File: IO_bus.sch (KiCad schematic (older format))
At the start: 3 parts, among them P10 CONN_01X08, P9 CONN_01X14

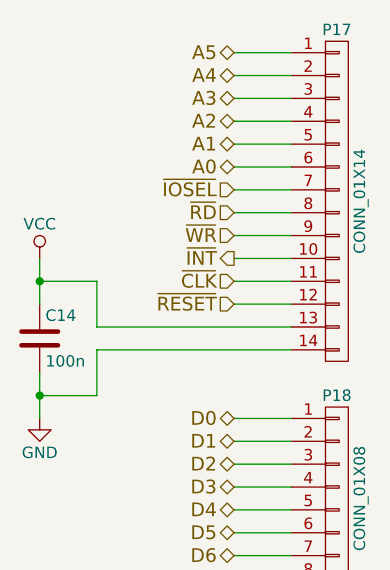
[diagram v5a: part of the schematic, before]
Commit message: Updated LEDs, added power supply options, added mounting holes in schematic.
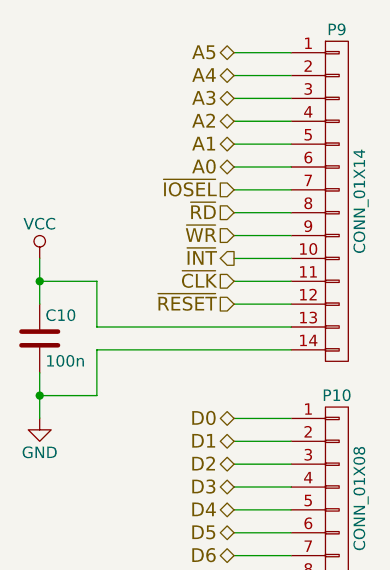
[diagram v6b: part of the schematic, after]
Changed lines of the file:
@@
 LIBS:microchip_pic18mcu
 LIBS:6850
+LIBS:nrc2016
 LIBS:z80-cache
 EELAYER 25 0
@@
 $Descr A4 11693 8268
 encoding utf-8
-Sheet 8 16
+Sheet 4 16
 Title ""
 Date ""
@@
 AR Path="/578460AE/57973E0B/57809978" Ref="P22"  Part="1"
 AR Path="/578460AE/57974892/57809978" Ref="P24"  Part="1"
-F 0 "P18" H 3700 4400 50  0000 C CNN
+F 0 "P10" H 3700 4400 50  0000 C CNN
 F 1 "CONN_01X08" V 3800 3950 50  0000 C CNN
 F 2 "Pin_Headers:Pin_Header_Straight_1x08" H 3700 3950 50  0001 C CNN
@@
 AR Path="/578460AE/57973E0B/5783B273" Ref="#PWR042"  Part="1"
 AR Path="/578460AE/57974892/5783B273" Ref="#PWR044"  Part="1"
-F 0 "#PWR044" H 2400 2750 50  0001 C CNN
+F 0 "#PWR030" H 2400 2750 50  0001 C CNN
 F 1 "VCC" H 2400 3050 50  0000 C CNN
 F 2 "" H 2400 2900 50  0000 C CNN
@@
 AR Path="/578460AE/57973E0B/5783B28B" Ref="#PWR043"  Part="1"
 AR Path="/578460AE/57974892/5783B28B" Ref="#PWR045"  Part="1"
-F 0 "#PWR045" H 2400 3350 50  0001 C CNN
+F 0 "#PWR031" H 2400 3350 50  0001 C CNN
 F 1 "GND" H 2400 3450 50  0000 C CNN
 F 2 "" H 2400 3600 50  0000 C CNN
@@
 AR Path="/578460AE/57973E0B/5783B2B3" Ref="C16"  Part="1"
 AR Path="/578460AE/57974892/5783B2B3" Ref="C17"  Part="1"
-F 0 "C14" H 2425 3350 50  0000 L CNN
+F 0 "C10" H 2425 3350 50  0000 L CNN
 F 1 "100n" H 2425 3150 50  0000 L CNN
 F 2 "Capacitors_SMD:C_0805_HandSoldering" H 2438 3100 50  0001 C CNN
@@
 AR Path="/578460AE/57973E0B/5796F695" Ref="P21"  Part="1"
 AR Path="/578460AE/57974892/5796F695" Ref="P23"  Part="1"
-F 0 "P17" H 3700 3400 50  0000 C CNN
+F 0 "P9" H 3700 3400 50  0000 C CNN
 F 1 "CONN_01X14" V 3800 2650 50  0000 C CNN
 F 2 "Socket_Strips:Socket_Strip_Straight_1x14" H 3700 2650 50  0001 C CNN

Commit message: Update PCB, better layout. Got Addr bus back in order
Think having both USB and DC input would be useful. Switchmode a plus
then plugpack/battery etc voltage doesn't matter. Plus I have a bag full
of those parts too!

I've refdes'd the linear reg just to deal with the net. Will remove if
we both are happy with switcher. Linear cheaper to kit out I guess.

Was trying to find a better way to combine USB and DC power rails than
just schottky diodes. If you have any ideas.

Going to have a big area under the IO ports, might be worth adding a USB
to serial, or sacrifice a IO port for some blinky LEDs and buttons?
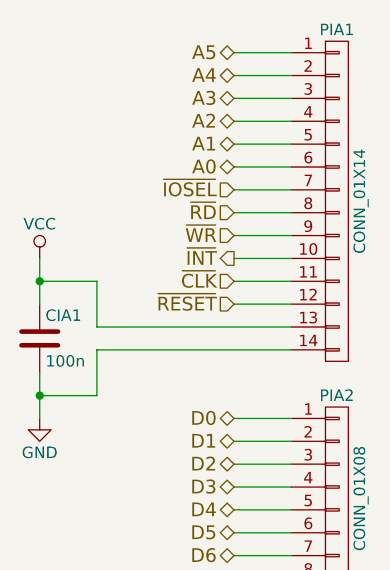
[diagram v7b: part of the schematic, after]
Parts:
- PIA2: renamed from P10; footprint Pin_Headers:Pin_Header_Straight_1x08 -> Socket_Strips:Socket_Strip_Straight_1x08
- renumbered C10 to CIA1, P9 to PIA1
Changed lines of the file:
@@
 	2650 3300 3500 3300
 $Comp
-L CONN_01X08 P10
+L CONN_01X08 PIA2
 U 1 1 57809978
 P 3700 3950
-AR Path="/578460AE/578087DE/57809978" Ref="P10"  Part="1"
-AR Path="/578460AE/57822535/57809978" Ref="P12"  Part="1"
-AR Path="/578460AE/57824229/57809978" Ref="P14"  Part="1"
-AR Path="/578460AE/57824279/57809978" Ref="P16"  Part="1"
-AR Path="/578460AE/578298A9/57809978" Ref="P18"  Part="1"
-AR Path="/578460AE/578298F9/57809978" Ref="P20"  Part="1"
-AR Path="/578460AE/57830D91/57809978" Ref="P22"  Part="1"
-AR Path="/578460AE/57831F66/57809978" Ref="P24"  Part="1"
-AR Path="/578460AE/57951EDB/57809978" Ref="P12"  Part="1"
-AR Path="/578460AE/57952CC1/57809978" Ref="P14"  Part="1"
-AR Path="/578460AE/579537DA/57809978" Ref="P16"  Part="1"
-AR Path="/578460AE/579543C3/57809978" Ref="P18"  Part="1"
-AR Path="/578460AE/57954FF1/57809978" Ref="P20"  Part="1"
-AR Path="/578460AE/57955FE5/57809978" Ref="P22"  Part="1"
-AR Path="/578460AE/57956D49/57809978" Ref="P24"  Part="1"
-AR Path="/578460AE/57970A38/57809978" Ref="P12"  Part="1"
-AR Path="/578460AE/57971583/57809978" Ref="P14"  Part="1"
-AR Path="/578460AE/579727D6/57809978" Ref="P16"  Part="1"
-AR Path="/578460AE/57972DE9/57809978" Ref="P18"  Part="1"
-AR Path="/578460AE/579734B0/57809978" Ref="P20"  Part="1"
-AR Path="/578460AE/57973E0B/57809978" Ref="P22"  Part="1"
-AR Path="/578460AE/57974892/57809978" Ref="P24"  Part="1"
-F 0 "P10" H 3700 4400 50  0000 C CNN
+AR Path="/578460AE/578087DE/57809978" Ref="PIA2"  Part="1"
+AR Path="/578460AE/57970A38/57809978" Ref="PIG2"  Part="1"
+AR Path="/578460AE/57971583/57809978" Ref="PIH2"  Part="1"
+AR Path="/578460AE/579727D6/57809978" Ref="PIB2"  Part="1"
+AR Path="/578460AE/57972DE9/57809978" Ref="PIC2"  Part="1"
+AR Path="/578460AE/579734B0/57809978" Ref="PID2"  Part="1"
+AR Path="/578460AE/57973E0B/57809978" Ref="PIE2"  Part="1"
+AR Path="/578460AE/57974892/57809978" Ref="PIF2"  Part="1"
+F 0 "PIA2" H 3700 4400 50  0000 C CNN
 F 1 "CONN_01X08" V 3800 3950 50  0000 C CNN
-F 2 "Pin_Headers:Pin_Header_Straight_1x08" H 3700 3950 50  0001 C CNN
+F 2 "Socket_Strips:Socket_Strip_Straight_1x08" H 3700 3950 50  0001 C CNN
 F 3 "" H 3700 3950 50  0000 C CNN
 	1    3700 3950
@@
 	2400 3400 2400 3600
 $Comp
-L VCC #PWR030
+L VCC #PWR041
 U 1 1 5783B273
 P 2400 2900
-AR Path="/578460AE/578087DE/5783B273" Ref="#PWR030"  Part="1"
-AR Path="/578460AE/57822535/5783B273" Ref="#PWR029"  Part="1"
-AR Path="/578460AE/57824229/5783B273" Ref="#PWR031"  Part="1"
-AR Path="/578460AE/57824279/5783B273" Ref="#PWR033"  Part="1"
-AR Path="/578460AE/578298A9/5783B273" Ref="#PWR035"  Part="1"
-AR Path="/578460AE/578298F9/5783B273" Ref="#PWR037"  Part="1"
-AR Path="/578460AE/57830D91/5783B273" Ref="#PWR039"  Part="1"
-AR Path="/578460AE/57831F66/5783B273" Ref="#PWR041"  Part="1"
-AR Path="/578460AE/57951EDB/5783B273" Ref="#PWR28"  Part="1"
-AR Path="/578460AE/57952CC1/5783B273" Ref="#PWR30"  Part="1"
-AR Path="/578460AE/579537DA/5783B273" Ref="#PWR32"  Part="1"
-AR Path="/578460AE/579543C3/5783B273" Ref="#PWR34"  Part="1"
-AR Path="/578460AE/57954FF1/5783B273" Ref="#PWR36"  Part="1"
-AR Path="/578460AE/57955FE5/5783B273" Ref="#PWR38"  Part="1"
-AR Path="/578460AE/57956D49/5783B273" Ref="#PWR40"  Part="1"
-AR Path="/578460AE/57970A38/5783B273" Ref="#PWR032"  Part="1"
-AR Path="/578460AE/57971583/5783B273" Ref="#PWR034"  Part="1"
-AR Path="/578460AE/579727D6/5783B273" Ref="#PWR036"  Part="1"
-AR Path="/578460AE/57972DE9/5783B273" Ref="#PWR038"  Part="1"
-AR Path="/578460AE/579734B0/5783B273" Ref="#PWR040"  Part="1"
-AR Path="/578460AE/57973E0B/5783B273" Ref="#PWR042"  Part="1"
-AR Path="/578460AE/57974892/5783B273" Ref="#PWR044"  Part="1"
-F 0 "#PWR030" H 2400 2750 50  0001 C CNN
+AR Path="/578460AE/578087DE/5783B273" Ref="#PWR041"  Part="1"
+AR Path="/578460AE/57970A38/5783B273" Ref="#PWR043"  Part="1"
+AR Path="/578460AE/57971583/5783B273" Ref="#PWR045"  Part="1"
+AR Path="/578460AE/579727D6/5783B273" Ref="#PWR047"  Part="1"
+AR Path="/578460AE/57972DE9/5783B273" Ref="#PWR049"  Part="1"
+AR Path="/578460AE/579734B0/5783B273" Ref="#PWR051"  Part="1"
+AR Path="/578460AE/57973E0B/5783B273" Ref="#PWR053"  Part="1"
+AR Path="/578460AE/57974892/5783B273" Ref="#PWR055"  Part="1"
+F 0 "#PWR055" H 2400 2750 50  0001 C CNN
 F 1 "VCC" H 2400 3050 50  0000 C CNN
 F 2 "" H 2400 2900 50  0000 C CNN
@@
 $EndComp
 $Comp
-L GND #PWR031
+L GND #PWR042
 U 1 1 5783B28B
 P 2400 3600
-AR Path="/578460AE/578087DE/5783B28B" Ref="#PWR031"  Part="1"
-AR Path="/578460AE/57822535/5783B28B" Ref="#PWR030"  Part="1"
-AR Path="/578460AE/57824229/5783B28B" Ref="#PWR032"  Part="1"
-AR Path="/578460AE/57824279/5783B28B" Ref="#PWR034"  Part="1"
-AR Path="/578460AE/578298A9/5783B28B" Ref="#PWR036"  Part="1"
-AR Path="/578460AE/578298F9/5783B28B" Ref="#PWR038"  Part="1"
-AR Path="/578460AE/57830D91/5783B28B" Ref="#PWR040"  Part="1"
-AR Path="/578460AE/57831F66/5783B28B" Ref="#PWR042"  Part="1"
-AR Path="/578460AE/57951EDB/5783B28B" Ref="#PWR29"  Part="1"
-AR Path="/578460AE/57952CC1/5783B28B" Ref="#PWR31"  Part="1"
-AR Path="/578460AE/579537DA/5783B28B" Ref="#PWR33"  Part="1"
-AR Path="/578460AE/579543C3/5783B28B" Ref="#PWR35"  Part="1"
-AR Path="/578460AE/57954FF1/5783B28B" Ref="#PWR37"  Part="1"
-AR Path="/578460AE/57955FE5/5783B28B" Ref="#PWR39"  Part="1"
-AR Path="/578460AE/57956D49/5783B28B" Ref="#PWR41"  Part="1"
-AR Path="/578460AE/57970A38/5783B28B" Ref="#PWR033"  Part="1"
-AR Path="/578460AE/57971583/5783B28B" Ref="#PWR035"  Part="1"
-AR Path="/578460AE/579727D6/5783B28B" Ref="#PWR037"  Part="1"
-AR Path="/578460AE/57972DE9/5783B28B" Ref="#PWR039"  Part="1"
-AR Path="/578460AE/579734B0/5783B28B" Ref="#PWR041"  Part="1"
-AR Path="/578460AE/57973E0B/5783B28B" Ref="#PWR043"  Part="1"
-AR Path="/578460AE/57974892/5783B28B" Ref="#PWR045"  Part="1"
-F 0 "#PWR031" H 2400 3350 50  0001 C CNN
+AR Path="/578460AE/578087DE/5783B28B" Ref="#PWR042"  Part="1"
+AR Path="/578460AE/57970A38/5783B28B" Ref="#PWR044"  Part="1"
+AR Path="/578460AE/57971583/5783B28B" Ref="#PWR046"  Part="1"
+AR Path="/578460AE/579727D6/5783B28B" Ref="#PWR048"  Part="1"
+AR Path="/578460AE/57972DE9/5783B28B" Ref="#PWR050"  Part="1"
+AR Path="/578460AE/579734B0/5783B28B" Ref="#PWR052"  Part="1"
+AR Path="/578460AE/57973E0B/5783B28B" Ref="#PWR054"  Part="1"
+AR Path="/578460AE/57974892/5783B28B" Ref="#PWR056"  Part="1"
+F 0 "#PWR056" H 2400 3350 50  0001 C CNN
 F 1 "GND" H 2400 3450 50  0000 C CNN
 F 2 "" H 2400 3600 50  0000 C CNN
@@
 $EndComp
 $Comp
-L C C10
+L C CIA1
 U 1 1 5783B2B3
 P 2400 3250
-AR Path="/578460AE/578087DE/5783B2B3" Ref="C10"  Part="1"
-AR Path="/578460AE/57822535/5783B2B3" Ref="C11"  Part="1"
-AR Path="/578460AE/57824229/5783B2B3" Ref="C12"  Part="1"
-AR Path="/578460AE/57824279/5783B2B3" Ref="C13"  Part="1"
-AR Path="/578460AE/578298A9/5783B2B3" Ref="C14"  Part="1"
-AR Path="/578460AE/578298F9/5783B2B3" Ref="C15"  Part="1"
-AR Path="/578460AE/57830D91/5783B2B3" Ref="C16"  Part="1"
-AR Path="/578460AE/57831F66/5783B2B3" Ref="C17"  Part="1"
-AR Path="/578460AE/57951EDB/5783B2B3" Ref="C10"  Part="1"
-AR Path="/578460AE/57952CC1/5783B2B3" Ref="C10"  Part="1"
-AR Path="/578460AE/579537DA/5783B2B3" Ref="C10"  Part="1"
-AR Path="/578460AE/579543C3/5783B2B3" Ref="C10"  Part="1"
-AR Path="/578460AE/57954FF1/5783B2B3" Ref="C10"  Part="1"
-AR Path="/578460AE/57955FE5/5783B2B3" Ref="C10"  Part="1"
-AR Path="/578460AE/57956D49/5783B2B3" Ref="C10"  Part="1"
-AR Path="/578460AE/57970A38/5783B2B3" Ref="C11"  Part="1"
-AR Path="/578460AE/57971583/5783B2B3" Ref="C12"  Part="1"
-AR Path="/578460AE/579727D6/5783B2B3" Ref="C13"  Part="1"
-AR Path="/578460AE/57972DE9/5783B2B3" Ref="C14"  Part="1"
-AR Path="/578460AE/579734B0/5783B2B3" Ref="C15"  Part="1"
-AR Path="/578460AE/57973E0B/5783B2B3" Ref="C16"  Part="1"
-AR Path="/578460AE/57974892/5783B2B3" Ref="C17"  Part="1"
-F 0 "C10" H 2425 3350 50  0000 L CNN
+AR Path="/578460AE/578087DE/5783B2B3" Ref="CIA1"  Part="1"
+AR Path="/578460AE/57970A38/5783B2B3" Ref="CIG1"  Part="1"
+AR Path="/578460AE/57971583/5783B2B3" Ref="CIH1"  Part="1"
+AR Path="/578460AE/579727D6/5783B2B3" Ref="CIB1"  Part="1"
+AR Path="/578460AE/57972DE9/5783B2B3" Ref="CIC1"  Part="1"
+AR Path="/578460AE/579734B0/5783B2B3" Ref="CID1"  Part="1"
+AR Path="/578460AE/57973E0B/5783B2B3" Ref="CIE1"  Part="1"
+AR Path="/578460AE/57974892/5783B2B3" Ref="CIF1"  Part="1"
+F 0 "CIA1" H 2425 3350 50  0000 L CNN
 F 1 "100n" H 2425 3150 50  0000 L CNN
 F 2 "Capacitors_SMD:C_0805_HandSoldering" H 2438 3100 50  0001 C CNN
@@
 Connection ~ 2400 3500
 $Comp
-L CONN_01X14 P9
+L CONN_01X14 PIA1
 U 1 1 5796F695
 P 3700 2650
-AR Path="/578460AE/578087DE/5796F695" Ref="P9"  Part="1"
-AR Path="/578460AE/57970A38/5796F695" Ref="P11"  Part="1"
-AR Path="/578460AE/57971583/5796F695" Ref="P13"  Part="1"
-AR Path="/578460AE/579727D6/5796F695" Ref="P15"  Part="1"
-AR Path="/578460AE/57972DE9/5796F695" Ref="P17"  Part="1"
-AR Path="/578460AE/579734B0/5796F695" Ref="P19"  Part="1"
-AR Path="/578460AE/57973E0B/5796F695" Ref="P21"  Part="1"
-AR Path="/578460AE/57974892/5796F695" Ref="P23"  Part="1"
-F 0 "P9" H 3700 3400 50  0000 C CNN
+AR Path="/578460AE/578087DE/5796F695" Ref="PIA1"  Part="1"
+AR Path="/578460AE/57970A38/5796F695" Ref="PIG1"  Part="1"
+AR Path="/578460AE/57971583/5796F695" Ref="PIH1"  Part="1"
+AR Path="/578460AE/579727D6/5796F695" Ref="PIB1"  Part="1"
+AR Path="/578460AE/57972DE9/5796F695" Ref="PIC1"  Part="1"
+AR Path="/578460AE/579734B0/5796F695" Ref="PID1"  Part="1"
+AR Path="/578460AE/57973E0B/5796F695" Ref="PIE1"  Part="1"
+AR Path="/578460AE/57974892/5796F695" Ref="PIF1"  Part="1"
+F 0 "PIA1" H 3700 3400 50  0000 C CNN
 F 1 "CONN_01X14" V 3800 2650 50  0000 C CNN
 F 2 "Socket_Strips:Socket_Strip_Straight_1x14" H 3700 2650 50  0001 C CNN

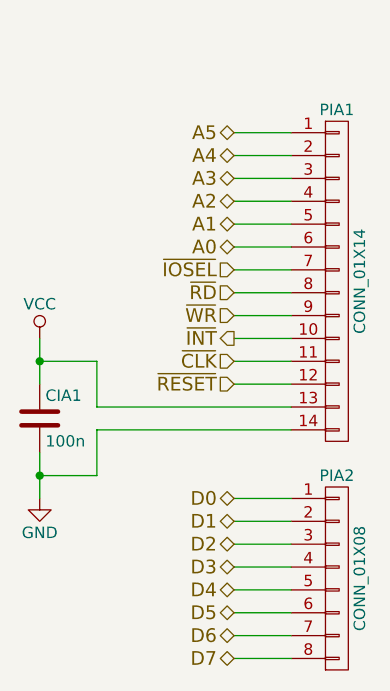
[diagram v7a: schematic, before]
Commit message: PCB layout complete, passes DRC, more tuning required
One thing not enough buffers for all address lines (missed A5), so
swapped out the CLK. Not sure if that was a good idea, but didn't want
to add another chip for a single buffer. :(
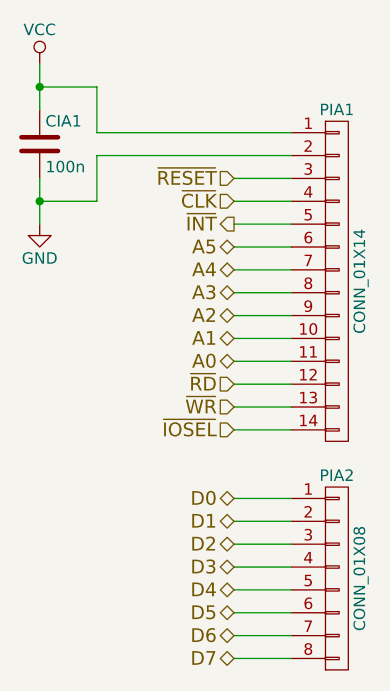
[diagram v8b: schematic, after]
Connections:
- net A0: now also PIA1.11 (P11); no longer PIA1.6 (P6)
- net A1: now also PIA1.10 (P10); no longer PIA1.5 (P5)
- net A2: now also PIA1.9 (P9); no longer PIA1.4 (P4)
- net A3: now also PIA1.8 (P8); no longer PIA1.3 (P3)
- net A4: now also PIA1.7 (P7); no longer PIA1.2 (P2)
- net A5: now also PIA1.6 (P6); no longer PIA1.1 (P1)
- net GND: now also PIA1.2 (P2); no longer PIA1.14 (P14)
- net VCC: now also PIA1.1 (P1); no longer PIA1.13 (P13)
- net ~CLK: now also PIA1.4 (P4); no longer PIA1.11 (P11)
- net ~INT: now also PIA1.5 (P5); no longer PIA1.10 (P10)
- net ~IOSEL: now also PIA1.14 (P14); no longer PIA1.7 (P7)
- net ~RD: now also PIA1.12 (P12); no longer PIA1.8 (P8)
- net ~RESET: now also PIA1.3 (P3); no longer PIA1.12 (P12)
- net ~WR: now also PIA1.13 (P13); no longer PIA1.9 (P9)
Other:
- moved on the sheet: CIA1
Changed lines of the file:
@@
 Comment4 ""
 $EndDescr
+Text HLabel 3250 3000 0    60   3State ~ 0
+A0
+Text HLabel 3250 2900 0    60   3State ~ 0
+A1
+Text HLabel 3250 2800 0    60   3State ~ 0
+A2
+Text HLabel 3250 2700 0    60   3State ~ 0
+A3
+Text HLabel 3250 2600 0    60   3State ~ 0
+A4
 Text HLabel 3250 2500 0    60   3State ~ 0
-A0
-Text HLabel 3250 2400 0    60   3State ~ 0
-A1
-Text HLabel 3250 2300 0    60   3State ~ 0
-A2
-Text HLabel 3250 2200 0    60   3State ~ 0
-A3
-Text HLabel 3250 2100 0    60   3State ~ 0
-A4
-Text HLabel 3250 2000 0    60   3State ~ 0
 A5
-Text HLabel 3250 2600 0    60   Input ~ 0
+Text HLabel 3250 3300 0    60   Input ~ 0
 ~IOSEL
-Text HLabel 3250 2700 0    60   Input ~ 0
+Text HLabel 3250 3100 0    60   Input ~ 0
 ~RD
-Text HLabel 3250 2800 0    60   Input ~ 0
+Text HLabel 3250 3200 0    60   Input ~ 0
 ~WR
-Text HLabel 3250 3000 0    60   Input ~ 0
+Text HLabel 3250 2300 0    60   Input ~ 0
 ~CLK
-Text HLabel 3250 2900 0    60   Output ~ 0
+Text HLabel 3250 2400 0    60   Output ~ 0
 ~INT
 Text HLabel 3250 4000 0    60   BiDi ~ 0
@@
 D3
 Wire Wire Line
-	3250 2000 3500 2000
-Wire Wire Line
-	3500 2100 3250 2100
-Wire Wire Line
-	3250 2200 3500 2200
-Wire Wire Line
-	3500 2300 3250 2300
-Wire Wire Line
 	3250 2400 3500 2400
 Wire Wire Line
@@
 	3250 2800 3500 2800
 Wire Wire Line
-	3250 2900 3500 2900
+	3500 2900 3250 2900
 Wire Wire Line
 	3250 3000 3500 3000
 Wire Wire Line
-	2650 3300 3500 3300
+	3500 3100 3250 3100
+Wire Wire Line
+	3250 3200 3500 3200
+Wire Wire Line
+	3250 3300 3500 3300
+Wire Wire Line
+	3250 2200 3500 2200
+Wire Wire Line
+	2650 2100 3500 2100
 $Comp
 L CONN_01X08 PIA2
@@
 Wire Wire Line
 	3500 4300 3250 4300
-Text HLabel 3250 3100 0    60   Input ~ 0
+Text HLabel 3250 2200 0    60   Input ~ 0
 ~RESET
 Wire Wire Line
-	3250 3100 3500 3100
+	3250 2300 3500 2300
 Wire Wire Line
-	2400 2900 2400 3100
+	2400 1700 2400 1900
 Wire Wire Line
-	2400 3400 2400 3600
+	2400 2200 2400 2400
 $Comp
-L VCC #PWR041
+L VCC #PWR035
 U 1 1 5783B273
-P 2400 2900
-AR Path="/578460AE/578087DE/5783B273" Ref="#PWR041"  Part="1"
-AR Path="/578460AE/57970A38/5783B273" Ref="#PWR043"  Part="1"
-AR Path="/578460AE/57971583/5783B273" Ref="#PWR045"  Part="1"
-AR Path="/578460AE/579727D6/5783B273" Ref="#PWR047"  Part="1"
-AR Path="/578460AE/57972DE9/5783B273" Ref="#PWR049"  Part="1"
-AR Path="/578460AE/579734B0/5783B273" Ref="#PWR051"  Part="1"
-AR Path="/578460AE/57973E0B/5783B273" Ref="#PWR053"  Part="1"
-AR Path="/578460AE/57974892/5783B273" Ref="#PWR055"  Part="1"
-F 0 "#PWR055" H 2400 2750 50  0001 C CNN
-F 1 "VCC" H 2400 3050 50  0000 C CNN
-F 2 "" H 2400 2900 50  0000 C CNN
-F 3 "" H 2400 2900 50  0000 C CNN
-	1    2400 2900
+P 2400 1700
+AR Path="/578460AE/578087DE/5783B273" Ref="#PWR035"  Part="1"
+AR Path="/578460AE/57970A38/5783B273" Ref="#PWR037"  Part="1"
+AR Path="/578460AE/57971583/5783B273" Ref="#PWR039"  Part="1"
+AR Path="/578460AE/579727D6/5783B273" Ref="#PWR041"  Part="1"
+AR Path="/578460AE/57972DE9/5783B273" Ref="#PWR043"  Part="1"
+AR Path="/578460AE/579734B0/5783B273" Ref="#PWR045"  Part="1"
+AR Path="/578460AE/57973E0B/5783B273" Ref="#PWR047"  Part="1"
+AR Path="/578460AE/57974892/5783B273" Ref="#PWR049"  Part="1"
+F 0 "#PWR035" H 2400 1550 50  0001 C CNN
+F 1 "VCC" H 2400 1850 50  0000 C CNN
+F 2 "" H 2400 1700 50  0000 C CNN
+F 3 "" H 2400 1700 50  0000 C CNN
+	1    2400 1700
 	1    0    0    -1
 $EndComp
 $Comp
-L GND #PWR042
+L GND #PWR036
 U 1 1 5783B28B
-P 2400 3600
-AR Path="/578460AE/578087DE/5783B28B" Ref="#PWR042"  Part="1"
-AR Path="/578460AE/57970A38/5783B28B" Ref="#PWR044"  Part="1"
-AR Path="/578460AE/57971583/5783B28B" Ref="#PWR046"  Part="1"
-AR Path="/578460AE/579727D6/5783B28B" Ref="#PWR048"  Part="1"
-AR Path="/578460AE/57972DE9/5783B28B" Ref="#PWR050"  Part="1"
-AR Path="/578460AE/579734B0/5783B28B" Ref="#PWR052"  Part="1"
-AR Path="/578460AE/57973E0B/5783B28B" Ref="#PWR054"  Part="1"
-AR Path="/578460AE/57974892/5783B28B" Ref="#PWR056"  Part="1"
-F 0 "#PWR056" H 2400 3350 50  0001 C CNN
-F 1 "GND" H 2400 3450 50  0000 C CNN
-F 2 "" H 2400 3600 50  0000 C CNN
-F 3 "" H 2400 3600 50  0000 C CNN
-	1    2400 3600
+P 2400 2400
+AR Path="/578460AE/578087DE/5783B28B" Ref="#PWR036"  Part="1"
+AR Path="/578460AE/57970A38/5783B28B" Ref="#PWR038"  Part="1"
+AR Path="/578460AE/57971583/5783B28B" Ref="#PWR040"  Part="1"
+AR Path="/578460AE/579727D6/5783B28B" Ref="#PWR042"  Part="1"
+AR Path="/578460AE/57972DE9/5783B28B" Ref="#PWR044"  Part="1"
+AR Path="/578460AE/579734B0/5783B28B" Ref="#PWR046"  Part="1"
+AR Path="/578460AE/57973E0B/5783B28B" Ref="#PWR048"  Part="1"
+AR Path="/578460AE/57974892/5783B28B" Ref="#PWR050"  Part="1"
+F 0 "#PWR036" H 2400 2150 50  0001 C CNN
+F 1 "GND" H 2400 2250 50  0000 C CNN
+F 2 "" H 2400 2400 50  0000 C CNN
+F 3 "" H 2400 2400 50  0000 C CNN
+	1    2400 2400
 	1    0    0    -1
 $EndComp
@@
 L C CIA1
 U 1 1 5783B2B3
-P 2400 3250
+P 2400 2050
 AR Path="/578460AE/578087DE/5783B2B3" Ref="CIA1"  Part="1"
 AR Path="/578460AE/57970A38/5783B2B3" Ref="CIG1"  Part="1"
@@
 AR Path="/578460AE/57973E0B/5783B2B3" Ref="CIE1"  Part="1"
 AR Path="/578460AE/57974892/5783B2B3" Ref="CIF1"  Part="1"
-F 0 "CIA1" H 2425 3350 50  0000 L CNN
-F 1 "100n" H 2425 3150 50  0000 L CNN
-F 2 "Capacitors_SMD:C_0805_HandSoldering" H 2438 3100 50  0001 C CNN
-F 3 "" H 2400 3250 50  0000 C CNN
-	1    2400 3250
+F 0 "CIA1" H 2425 2150 50  0000 L CNN
+F 1 "100n" H 2425 1950 50  0000 L CNN
+F 2 "Capacitors_SMD:C_0805_HandSoldering" H 2438 1900 50  0001 C CNN
+F 3 "" H 2400 2050 50  0000 C CNN
+	1    2400 2050
 	1    0    0    -1
 $EndComp
 Wire Wire Line
-	3500 3200 2650 3200
+	3500 2000 2650 2000
 Wire Wire Line
-	2650 3200 2650 3000
+	2650 2000 2650 1800
 Wire Wire Line
-	2650 3000 2400 3000
-Connection ~ 2400 3000
+	2650 1800 2400 1800
+Connection ~ 2400 1800
 Wire Wire Line
-	2650 3300 2650 3500
+	2650 2100 2650 2300
 Wire Wire Line
-	2650 3500 2400 3500
-Connection ~ 2400 3500
+	2650 2300 2400 2300
+Connection ~ 2400 2300
 $Comp
 L CONN_01X14 PIA1
